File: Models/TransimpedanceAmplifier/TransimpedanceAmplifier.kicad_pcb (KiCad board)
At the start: 2 copper layers, 107 parts, among them J1 Conn_01x02_Socket, J10 Conn_01x02_Pin, J11 Conn_01x24_Socket, J14 Conn_01x24_Socket, J2 Conn_01x02_Socket, J3 Conn_01x03_Pin, J4 Conn_01x02_Pin, J5 Conn_01x02_Pin, J6 Conn_01x02_Pin, J7 Conn_01x02_Pin, J8 Conn_01x02_Pin, J9 Conn_01x02_Pin, Q1 Q_PNP, Q2 Q_NPN, U1 LM7905, -5V, 5%, U10 DAC81401, U11 ISO7641FM, U12 ISO7641FM, U13 ADS8699, U2 LM7805, 5V, 5%, U3 OPA828, U4 AD8615, U5 OP37GPZ, U6 LM7915, -15V, 5%, U7 LM7815, 15V, 5%, U8 LM7805, 5V, 5%, U9 TLV76133, 3.3V, 1%

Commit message: Let's hope this setup works
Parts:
- moved D8 39.7 mm to (127.0, 146.9), turned to 0 degrees
- moved C18 36.8 mm to (127.0, 149.2), turned to 0 degrees
- moved C17 30.4 mm to (131.2, 149.3), turned to 180 degrees
- moved U7 29.6 mm to (129.2, 152.5), turned to 180 degrees
- moved Q2 29.5 mm to (87.5, 126.9)
- moved R17 29.3 mm to (91.3, 128.2)
- moved D7 29.2 mm to (95.0, 126.9)
- moved D6 29.0 mm to (98.9, 126.9)
- moved R16 28.9 mm to (102.8, 128.2)
- moved Q1 28.8 mm to (106.5, 126.9), turned to -90 degrees
- moved R14 28.5 mm to (111.9, 127.3), turned to -90 degrees
- moved D4 26.2 mm to (109.7, 126.2), turned to -90 degrees
- moved D5 25.2 mm to (84.4, 126.2), turned to 90 degrees
- moved R15 24.4 mm to (82.2, 127.3), turned to -90 degrees
- moved BT1 0.32 mm to (120.2, 91.2)
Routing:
- net /TIA_TwoStage/PostAmplifier/Clamped_Output: track 29.7 -> 0.00 mm
- net Net-(D7-*): track 13.2 -> 0.00 mm
- net Net-(D6-K): track 10.8 -> 0.00 mm
- net /TIA_TwoStage/Output: track 43.5 -> 35.9 mm, vias 2 -> 0
- net Net-(D4-K): track 5.37 -> 0.00 mm
- net Net-(D5-A): track 3.14 -> 0.00 mm
- net Net-(D5-K): track 3.10 -> 0.00 mm
- net Net-(D4-A): track 3.10 -> 0.00 mm
- net (no net): track 1.71 -> 0.00 mm, vias 2 -> 0

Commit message: Wired that up, looks good
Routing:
- net /TIA_TwoStage/Output: track 35.9 -> 75.6 mm, vias 0 -> 2
- net /TIA_TwoStage/PostAmplifier/Clamped_Output: track 0.00 -> 38.4 mm
- net Net-(D6-K): track 0.00 -> 12.8 mm
- net Net-(D7-*): track 0.00 -> 9.73 mm
- net GND: track 126.2 -> 133.3 mm, vias 26 -> 29
- net Net-(D4-K): track 0.00 -> 4.74 mm
- net Net-(D5-A): track 0.00 -> 2.69 mm
- net Net-(D4-A): track 0.00 -> 2.22 mm
- net Net-(D5-K): track 0.00 -> 2.22 mm

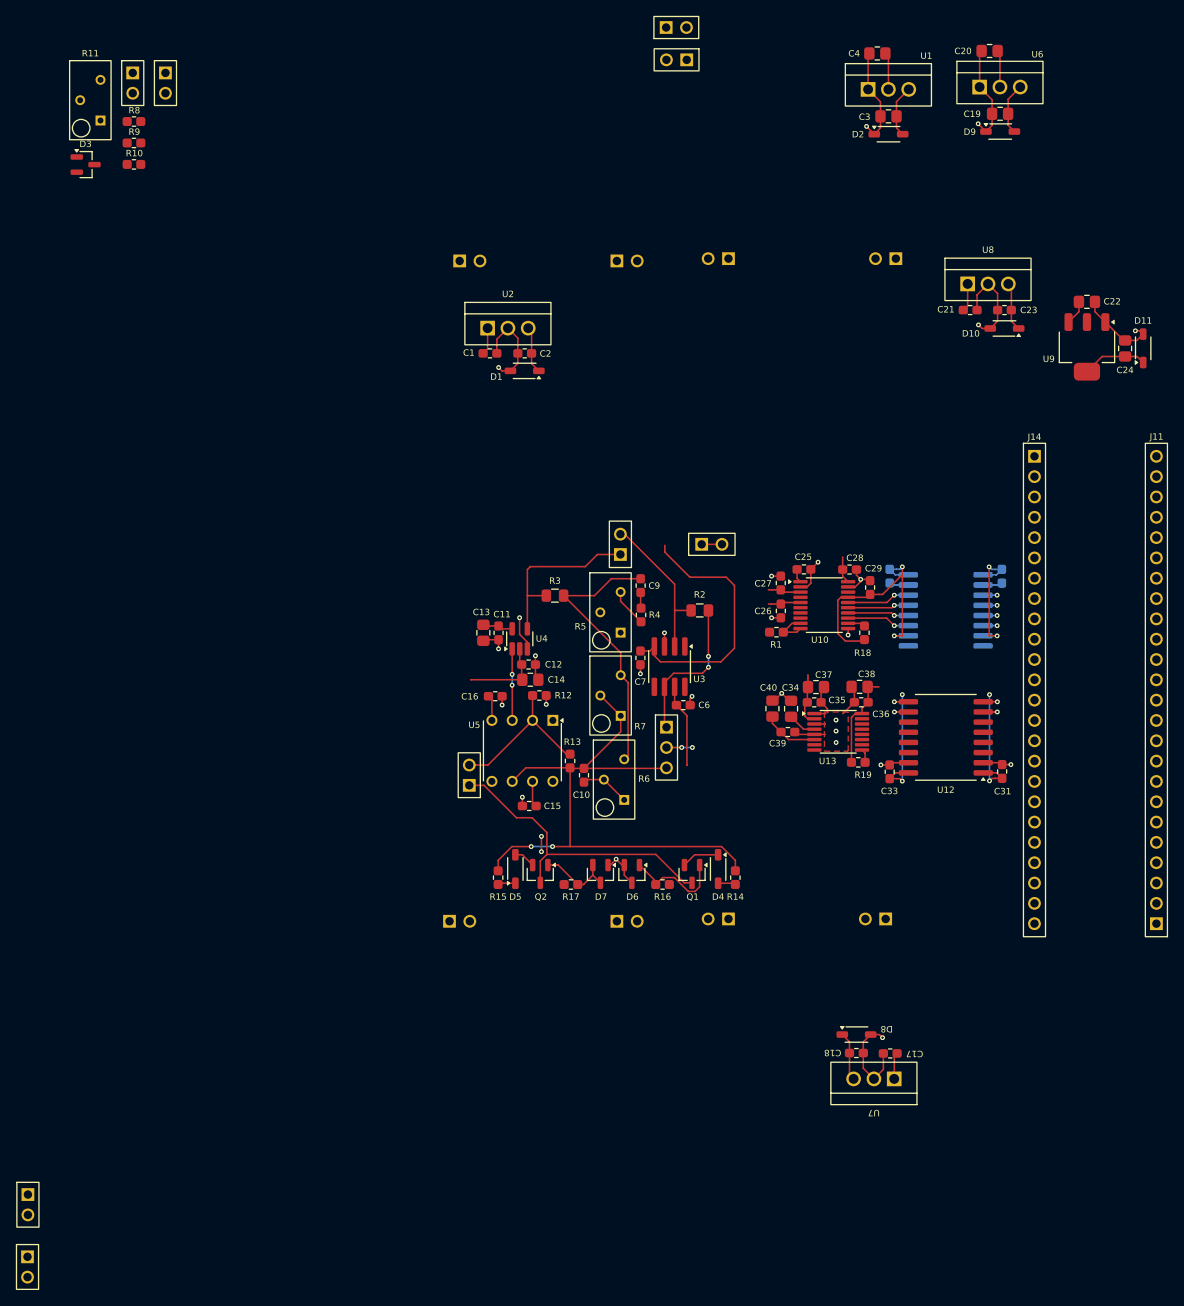
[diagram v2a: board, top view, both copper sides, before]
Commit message: Used 2.54 mm grid paradigm to position these jumper headers
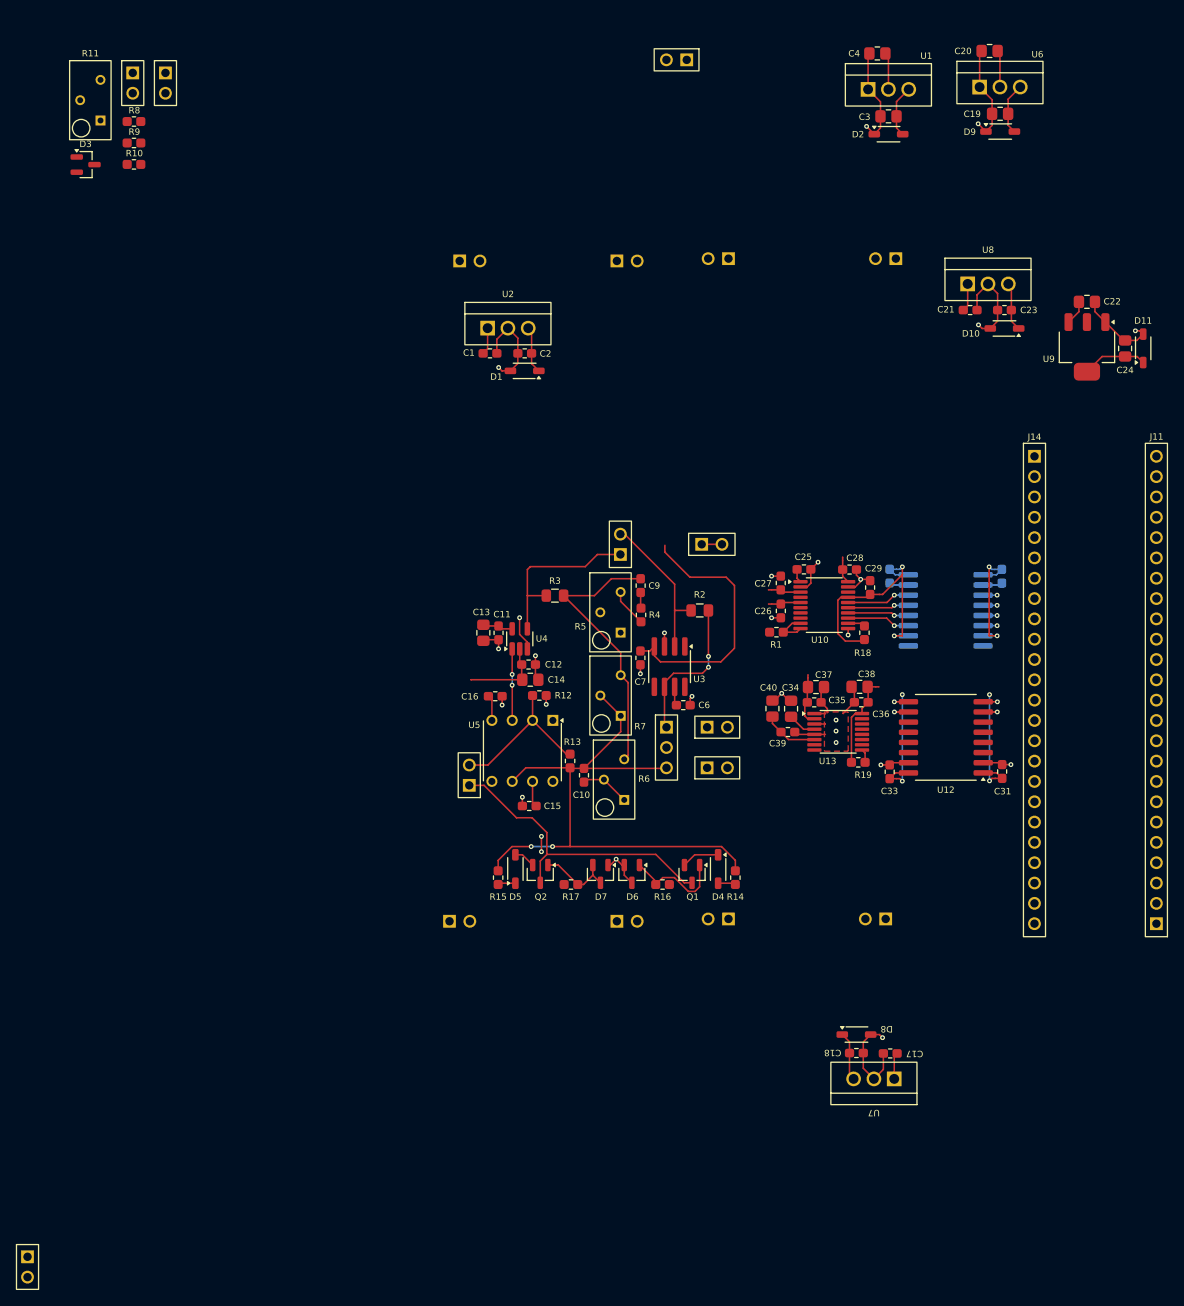
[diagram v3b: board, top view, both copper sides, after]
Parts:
- moved J8 102.0 mm to (109.6, 113.6), turned to 90 degrees
- moved J4 87.6 mm to (109.6, 108.5)
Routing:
- net /TIA_OneStage/V+: track 10.5 -> 2.39 mm
- net /CPU/ADC_Input: track 3.24 -> 0.00 mm, vias 2 -> 0
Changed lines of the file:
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@@
 	)
 	(footprint "Connector_Custom:PinHeader_1x2"
+		(locked yes)
 		(layer "F.Cu")
-		(at 104.49 21.06 90)
+		(at 109.61 108.52 90)
 		(property "Reference" "J4"
 			(at 0 3.66 270)
@@
 	)
 	(footprint "Connector_Custom:PinHeader_1x2"
+		(locked yes)
 		(layer "F.Cu")
-		(at 23.44 168.21)
+		(at 109.61 113.6 90)
 		(property "Reference" "J8"
-			(at 0.0025 -3.5625 0)
+			(at 0.0025 -3.5625 90)
 			(unlocked yes)
 			(layer "F.SilkS")
@@
 		)
 		(property "Value" "Conn_01x02_Pin"
-			(at 0.0025 -2.3625 0)
+			(at 0.0025 -2.3625 90)
 			(unlocked yes)
 			(layer "F.Fab")
@@
 		)
 		(property "Datasheet" "~"
-			(at 0 0 0)
+			(at 0 0 90)
 			(unlocked yes)
 			(layer "F.Fab")
@@
 		)
 		(property "Description" "Generic connector, single row, 01x02, script generated"
-			(at 0 0 0)
+			(at 0 0 90)
 			(unlocked yes)
 			(layer "F.Fab")
@@
 		)
 		(property "Purchase Link" "https://www.digikey.com/en/products/detail/sullins-connector-solutions/QPC02SXGN-RC/2618262"
-			(at 0 0 0)
+			(at 0 0 90)
 			(unlocked yes)
 			(layer "F.Fab")
@@
 		)
 		(property "Cost" "$0.10"
-			(at 0 0 0)
+			(at 0 0 90)
 			(unlocked yes)
 			(layer "F.Fab")
@@
 		)
 		(property "RoHS Compliant" "YES"
-			(at 0 0 0)
+			(at 0 0 90)
 			(unlocked yes)
 			(layer "F.Fab")
@@
 		)
 		(property "Cost (qty10)" "$0.025"
-			(at 0 0 0)
+			(at 0 0 90)
 			(unlocked yes)
 			(layer "F.Fab")
@@
 		)
 		(fp_text user "${REFERENCE}"
-			(at 0.0025 -1.1625 0)
+			(at 0.0025 -1.1625 90)
 			(unlocked yes)
 			(layer "F.Fab")
@@
 		)
 		(pad "1" thru_hole rect
-			(at 0 -1.27)
+			(at 0 -1.27 90)
 			(size 1.6 1.6)
 			(drill 1.05)
@@
 		)
 		(pad "2" thru_hole circle
-			(at 0 1.27)
+			(at 0 1.27 90)
 			(size 1.6 1.6)
 			(drill 1.05)
@@
 	)
 	(segment
-		(start 105.82 107.08)
-		(end 105.82 113.29)
-		(width 0.2)
-		(layer "F.Cu")
-		(net 14)
-	)
-	(segment
-		(start 104.505 105.765)
-		(end 105.82 107.08)
+		(start 104.2825 105.545)
+		(end 104.5025 105.765)
 		(width 0.2)
 		(layer "F.Cu")
@@
 	)
 	(segment
-		(start 104.5025 105.765)
-		(end 104.5025 105.7825)
-		(width 0.2)
-		(layer "F.Cu")
-		(net 14)
-	)
-	(segment
-		(start 105.82 113.29)
-		(end 105.81 113.3)
-		(width 0.2)
-		(layer "F.Cu")
-		(net 14)
-	)
-	(segment
-		(start 104.2825 105.545)
-		(end 104.5025 105.765)
-		(width 0.2)
-		(layer "F.Cu")
-		(net 14)
-	)
-	(segment
 		(start 102.512501 100.35)
 		(end 110.06 100.35)
@@
 	)
 	(segment
-		(start 103.26 111.06)
-		(end 105.16 111.06)
-		(width 0.2)
-		(layer "F.Cu")
-		(net 50)
-	)
-	(via
-		(at 105.16 111.06)
-		(size 0.6)
-		(drill 0.3)
-		(layers "F.Cu" "B.Cu")
-		(net 50)
-	)
-	(via
-		(at 106.5 111.06)
-		(size 0.6)
-		(drill 0.3)
-		(layers "F.Cu" "B.Cu")
-		(net 50)
-	)
-	(segment
-		(start 105.16 111.06)
-		(end 106.5 111.06)
-		(width 0.2)
-		(layer "B.Cu")
-		(net 50)
-	)
-	(segment

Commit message: Finalized a few more details
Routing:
- net /TIA_TwoStage/PostAmplifier/V+: track 3.27 -> 26.7 mm
- net /15V: track 9.50 -> 32.1 mm
- net /CPU/ADC_Input: track 0.00 -> 18.6 mm, vias 0 -> 2
- net Net-(J1-Pin_1): track 2.54 -> 17.4 mm, vias 0 -> 2
- net /TIA_OneStage/V+: track 2.39 -> 7.36 mm
- net GND: track 133.3 -> 134.8 mm, vias 29 -> 30
- net /TIA_TwoStage/Output: vias 2 -> 4
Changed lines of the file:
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@@
 	)
 	(footprint "TwoTerminal:SOD-123"
+		(locked yes)
 		(layer "F.Cu")
 		(at 84.373666 126.245 90)
@@
 	)
 	(footprint "TwoTerminal:RESC0603"
+		(locked yes)
 		(layer "F.Cu")
 		(at 102.770333 128.185 180)
@@
 	)
 	(footprint "ThreeTerminal:SOT-23"
+		(locked yes)
 		(layer "F.Cu")
 		(at 95.004666 126.86 -90)
@@
 	)
 	(footprint "TwoTerminal:RESC0603"
+		(locked yes)
 		(layer "F.Cu")
 		(at 91.319333 128.185 180)
@@
 	)
 	(footprint "ThreeTerminal:SOT-23"
+		(locked yes)
 		(layer "F.Cu")
 		(at 106.455666 126.86 -90)
@@
 	)
 	(footprint "TwoTerminal:SOD-123"
+		(locked yes)
 		(layer "F.Cu")
 		(at 109.716 126.245 -90)
@@
 	)
 	(footprint "ThreeTerminal:SOT-23"
+		(locked yes)
 		(layer "F.Cu")
 		(at 98.935 126.86 -90)
@@
 	)
 	(footprint "TwoTerminal:RESC0603"
+		(locked yes)
 		(layer "F.Cu")
 		(at 82.218333 127.325 -90)
@@
 	)
 	(footprint "TwoTerminal:RESC0603"
+		(locked yes)
 		(layer "F.Cu")
 		(at 111.871333 127.325 -90)
@@
 	)
 	(footprint "ThreeTerminal:SOT-23"
+		(locked yes)
 		(layer "F.Cu")
 		(at 87.484 126.86 -90)
@@
 	)
 	(segment
+		(start 120.29071 111.36929)
+		(end 120.29 111.37)
+		(width 0.2)
+		(layer "F.Cu")
+		(net 5)
+	)
+	(segment
 		(start 131.16 113.235)
 		(end 130.06 113.235)
@@
 	)
 	(segment
+		(start 121.7475 111.36929)
+		(end 120.29071 111.36929)
+		(width 0.2)
+		(layer "F.Cu")
+		(net 5)
+	)
+	(segment
 		(start 142.4025 24.24125)
 		(end 142.65 23.99375)
@@
 	)
 	(via
+		(at 120.29 111.37)
+		(size 0.6)
+		(drill 0.3)
+		(layers "F.Cu" "B.Cu")
+		(net 5)
+	)
+	(via
 		(at 86.88 99.5875)
 		(size 0.6)
@@
 	)
 	(segment
+		(start 114.429 94.721)
+		(end 116.025 93.125)
+		(width 0.2)
+		(layer "F.Cu")
+		(net 10)
+	)
+	(segment
+		(start 110.88 108.52)
+		(end 110.88 113.6)
+		(width 0.2)
+		(layer "F.Cu")
+		(net 10)
+	)
+	(segment
 		(start 126.14 151.97)
 		(end 126.65 152.48)
@@
 	)
 	(segment
+		(start 110.88 101)
+		(end 114.429 97.451)
+		(width 0.2)
+		(layer "F.Cu")
+		(net 10)
+	)
+	(segment
+		(start 114.429 97.451)
+		(end 114.429 94.721)
+		(width 0.2)
+		(layer "F.Cu")
+		(net 10)
+	)
+	(segment
 		(start 80.9 61.23)
 		(end 80.34 61.79)
@@
 	)
 	(segment
+		(start 110.88 108.52)
+		(end 110.88 101)
+		(width 0.2)
+		(layer "F.Cu")
+		(net 10)
+	)
+	(segment
 		(start 86.4 59.06)
 		(end 85.98 58.64)
@@
 	)
 	(segment
+		(start 104.5025 105.765)
+		(end 107.2575 108.52)
+		(width 0.2)
+		(layer "F.Cu")
+		(net 14)
+	)
+	(segment
+		(start 107.2575 108.52)
+		(end 108.34 108.52)
+		(width 0.2)
+		(layer "F.Cu")
+		(net 14)
+	)
+	(segment
 		(start 104.2825 105.545)
 		(end 104.5025 105.765)
@@
 	)
 	(segment
+		(start 91.21 119.19)
+		(end 91.21 123.44)
+		(width 0.2)
+		(layer "F.Cu")
+		(net 18)
+	)
+	(segment
 		(start 91.2875 113.67)
 		(end 91.21 113.5925)
@@
 	)
 	(segment
-		(start 91.21 113.5925)
-		(end 91.21 123.44)
-		(width 0.2)
-		(layer "F.Cu")
-		(net 18)
-	)
-	(segment
 		(start 110.140878 123.44)
 		(end 91.21 123.44)
@@
 	)
 	(segment
+		(start 91.21 113.5925)
+		(end 91.21 117.9)
+		(width 0.2)
+		(layer "F.Cu")
+		(net 18)
+	)
+	(segment
 		(start 91.21 123.44)
 		(end 89.02 123.44)
@@
 	)
 	(via
+		(at 91.21 119.19)
+		(size 0.6)
+		(drill 0.3)
+		(layers "F.Cu" "B.Cu")
+		(net 18)
+	)
+	(via
+		(at 91.21 117.9)
+		(size 0.6)
+		(drill 0.3)
+		(layers "F.Cu" "B.Cu")
+		(net 18)
+	)
+	(via
 		(at 86.35 123.44)
 		(size 0.6)
@@
 	)
 	(segment
+		(start 91.21 117.9)
+		(end 91.21 119.19)
+		(width 0.2)
+		(layer "B.Cu")
+		(net 18)
+	)
+	(segment
 		(start 89.02 123.44)
 		(end 86.35 123.44)
@@
 	)
 	(segment
+		(start 103.409 118.531)
+		(end 108.34 113.6)
+		(width 0.2)
+		(layer "F.Cu")
+		(net 22)
+	)
+	(segment
 		(start 86.52 115.29)
 		(end 86.52 117.9225)
@@
 	)
 	(segment
+		(start 86.9675 118.37)
+		(end 87.1285 118.531)
+		(width 0.2)
+		(layer "F.Cu")
+		(net 22)
+	)
+	(segment
+		(start 87.1285 118.531)
+		(end 103.409 118.531)
+		(width 0.2)
+		(layer "F.Cu")
+		(net 22)
+	)
+	(segment
 		(start 81.44 105.0925)
 		(end 80.9975 104.65)
@@
 	)
 	(segment
+		(start 113.04 88.5)
+		(end 110.2 85.66)
+		(width 0.2)
+		(layer "F.Cu")
+		(net 47)
+	)
+	(segment
+		(start 113.04 95.89)
+		(end 113.04 88.5)
+		(width 0.2)
+		(layer "F.Cu")
+		(net 47)
+	)
+	(segment
+		(start 113.8 96.65)
+		(end 113.04 95.89)
+		(width 0.2)
+		(layer "F.Cu")
+		(net 47)
+	)
+	(segment
+		(start 116.1525 96.645)
+		(end 115.035 96.645)
+		(width 0.2)
+		(layer "F.Cu")
+		(net 47)
+	)
+	(segment
+		(start 115.035 96.645)
+		(end 115.03 96.65)
+		(width 0.2)
+		(layer "F.Cu")
+		(net 47)
+	)
+	(via
+		(at 113.8 96.65)
+		(size 0.6)
+		(drill 0.3)
+		(layers "F.Cu" "B.Cu")
+		(net 47)
+	)
+	(via
+		(at 115.03 96.65)
+		(size 0.6)
+		(drill 0.3)
+		(layers "F.Cu" "B.Cu")
+		(net 47)
+	)
+	(segment
+		(start 115.03 96.65)
+		(end 113.8 96.65)
+		(width 0.2)
+		(layer "B.Cu")
+		(net 47)
+	)
+	(segment
 		(start 85.87 92.0775)
 		(end 85.87 88.82)
@@
 	)
 	(segment
+		(start 103.26 111.06)
+		(end 110.2 111.06)
+		(width 0.2)
+		(layer "F.Cu")
+		(net 50)
+	)
+	(segment
+		(start 111.55 111.06)
+		(end 119.63 111.06)
+		(width 0.2)
+		(layer "F.Cu")
+		(net 50)
+	)
+	(segment
+		(start 119.97071 110.71929)
+		(end 121.7475 110.71929)
+		(width 0.2)
+		(layer "F.Cu")
+		(net 50)
+	)
+	(segment
+		(start 119.63 111.06)
+		(end 119.97071 110.71929)
+		(width 0.2)
+		(layer "F.Cu")
+		(net 50)
+	)
+	(via
+		(at 110.2 111.06)
+		(size 0.6)
+		(drill 0.3)
+		(layers "F.Cu" "B.Cu")
+		(net 50)
+	)
+	(via
+		(at 111.55 111.06)
+		(size 0.6)
+		(drill 0.3)
+		(layers "F.Cu" "B.Cu")
+		(net 50)
+	)
+	(segment
+		(start 110.2 111.06)
+		(end 111.55 111.06)
+		(width 0.2)
+		(layer "B.Cu")
+		(net 50)
+	)
+	(segment
